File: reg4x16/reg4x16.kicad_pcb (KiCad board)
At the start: 2 copper layers, 34.1 x 59 mm, 20 parts, among them J1 Conn_01x04, J2 Conn_01x01, J3 Conn_02x15_Odd_Even, U1 74LS670, U2 74LS670, U3 74LS670, U4 74LS670, U5 74AHC1G32, U6 74AHC1G32

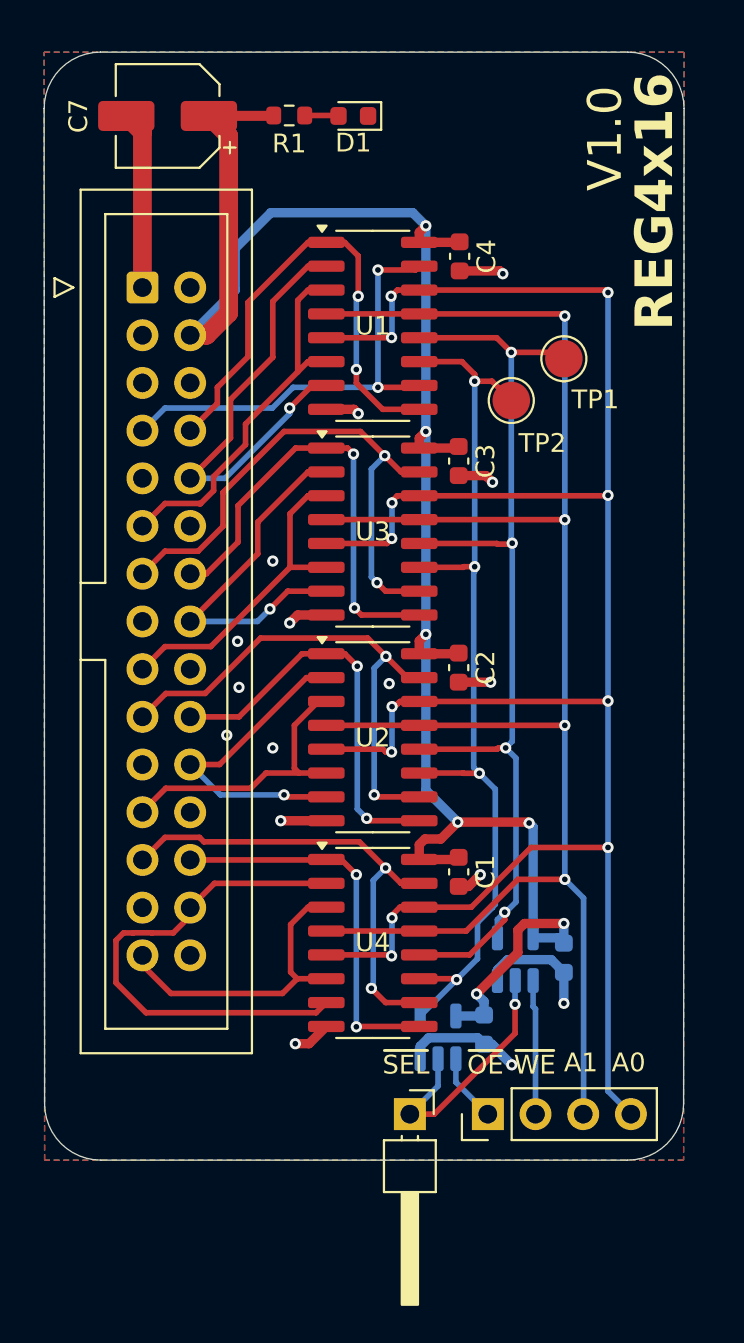
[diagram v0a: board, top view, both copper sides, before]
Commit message: Refactored files, finalized reg4x16, and used lowercase v
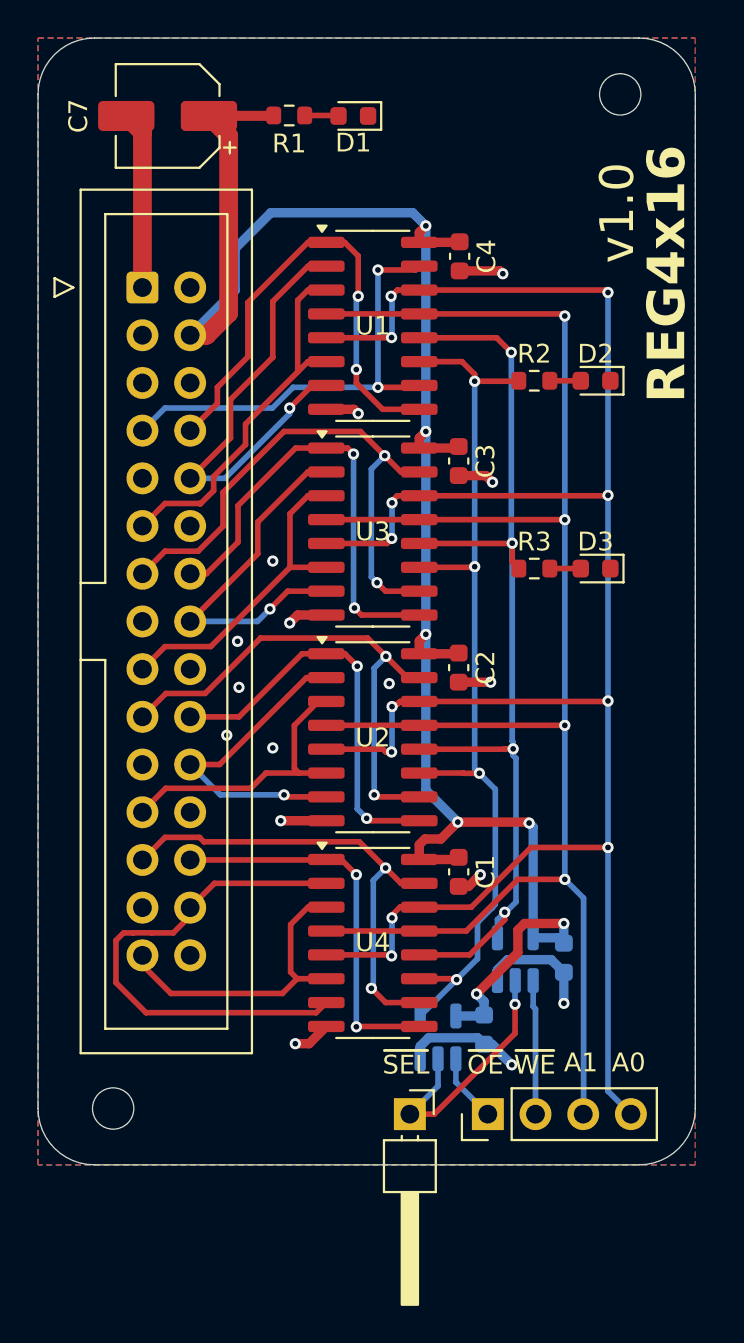
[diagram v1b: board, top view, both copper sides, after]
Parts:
- removed TP1, TP2: TestPoint, TestPoint:TestPoint_Pad_D2.0mm
- added D2: LED, LED_SMD:LED_0603_1608Metric, F.Cu at (49.2, 36.8)
- added D3: LED, LED_SMD:LED_0603_1608Metric, F.Cu at (49.2, 46.8)
- added H1: MountingHole, MountingHole:MountingHole_2.2mm_M2, F.Cu at (50.5, 21.5)
- added H2: MountingHole, MountingHole:MountingHole_2.2mm_M2, F.Cu at (23.5, 75.5)
- added R2: 220, Resistor_SMD:R_0603_1608Metric, F.Cu at (45.9, 36.8)
- added R3: 220, Resistor_SMD:R_0603_1608Metric, F.Cu at (45.9, 46.8)
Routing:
- net Net-(D3-A): track 0.00 -> 1.65 mm
- net Net-(D2-A): track 0.00 -> 1.65 mm
- net /s~{WE}: track 55.5 -> 54.1 mm
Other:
- board size 34.1 x 59 mm -> 35 x 60 mm
- board text added: "v1.0"
- board text removed: "V1.0"
